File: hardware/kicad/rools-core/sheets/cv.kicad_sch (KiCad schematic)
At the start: 56 parts, among them U4 OPA4171, U5 MCP6004, U6 LM4040DBZ-10, U9 DAC8565

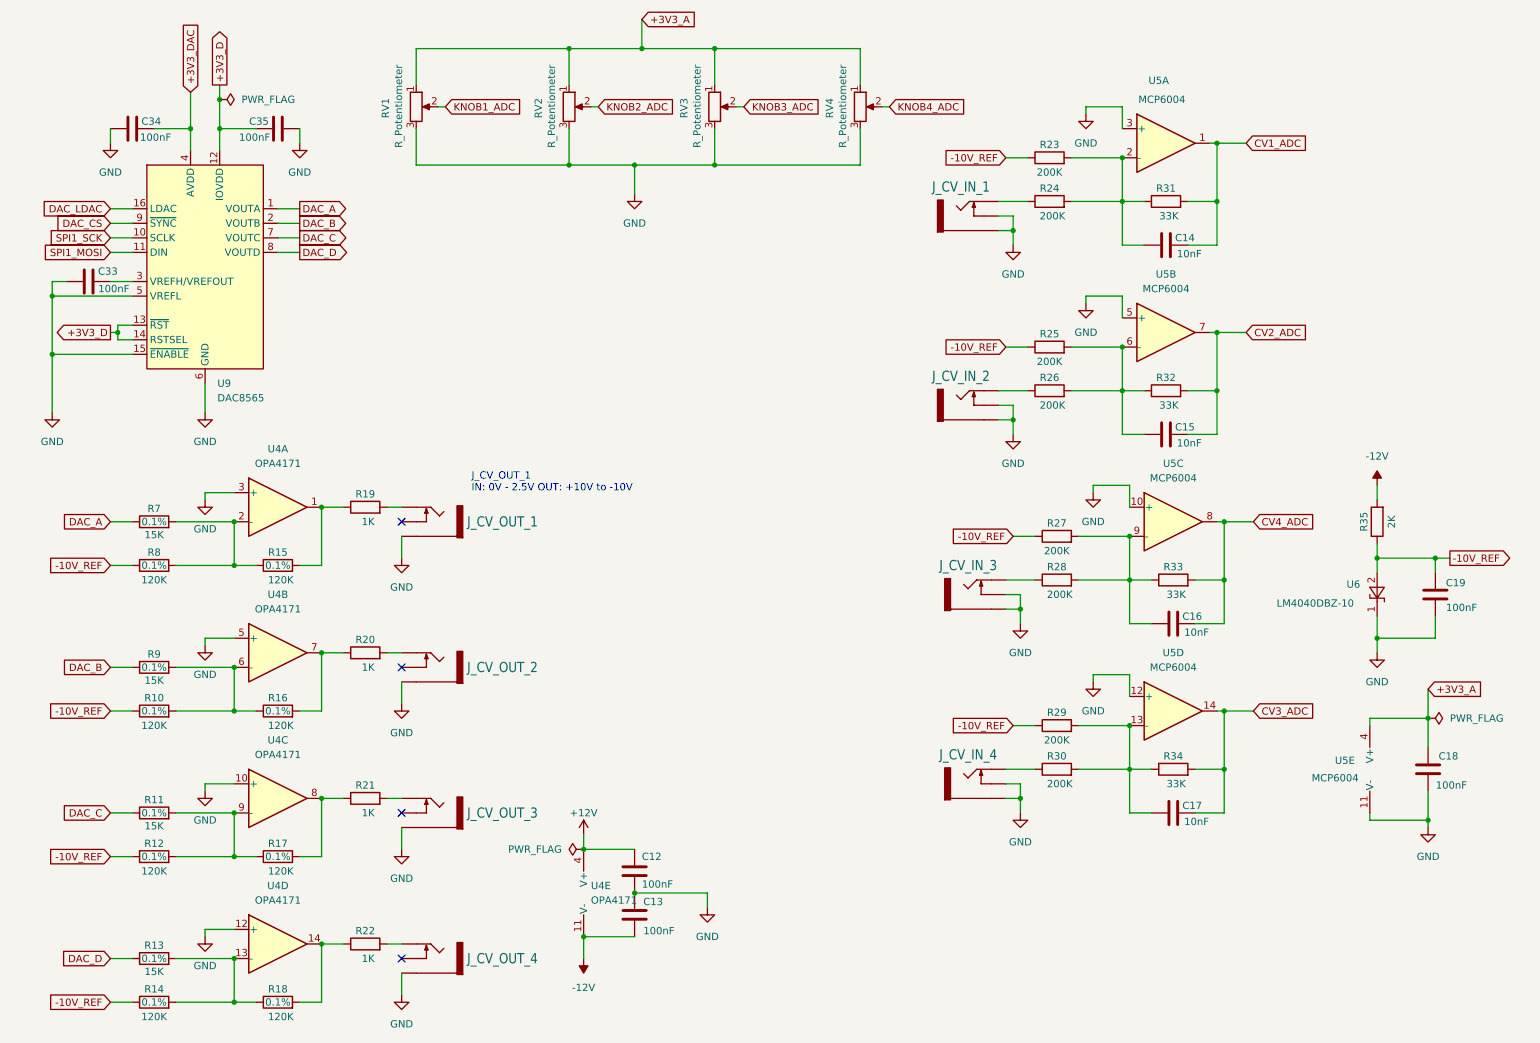
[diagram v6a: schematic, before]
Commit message: Lay out Core front-panel PCB for 10HP Eurorack fit.
Use RK09L 3-pin no-MP pots, split Daisy daughterboard, audio jack refs, and local display footprint library.

Co-authored-by: Cursor <cursoragent@cursor.com>
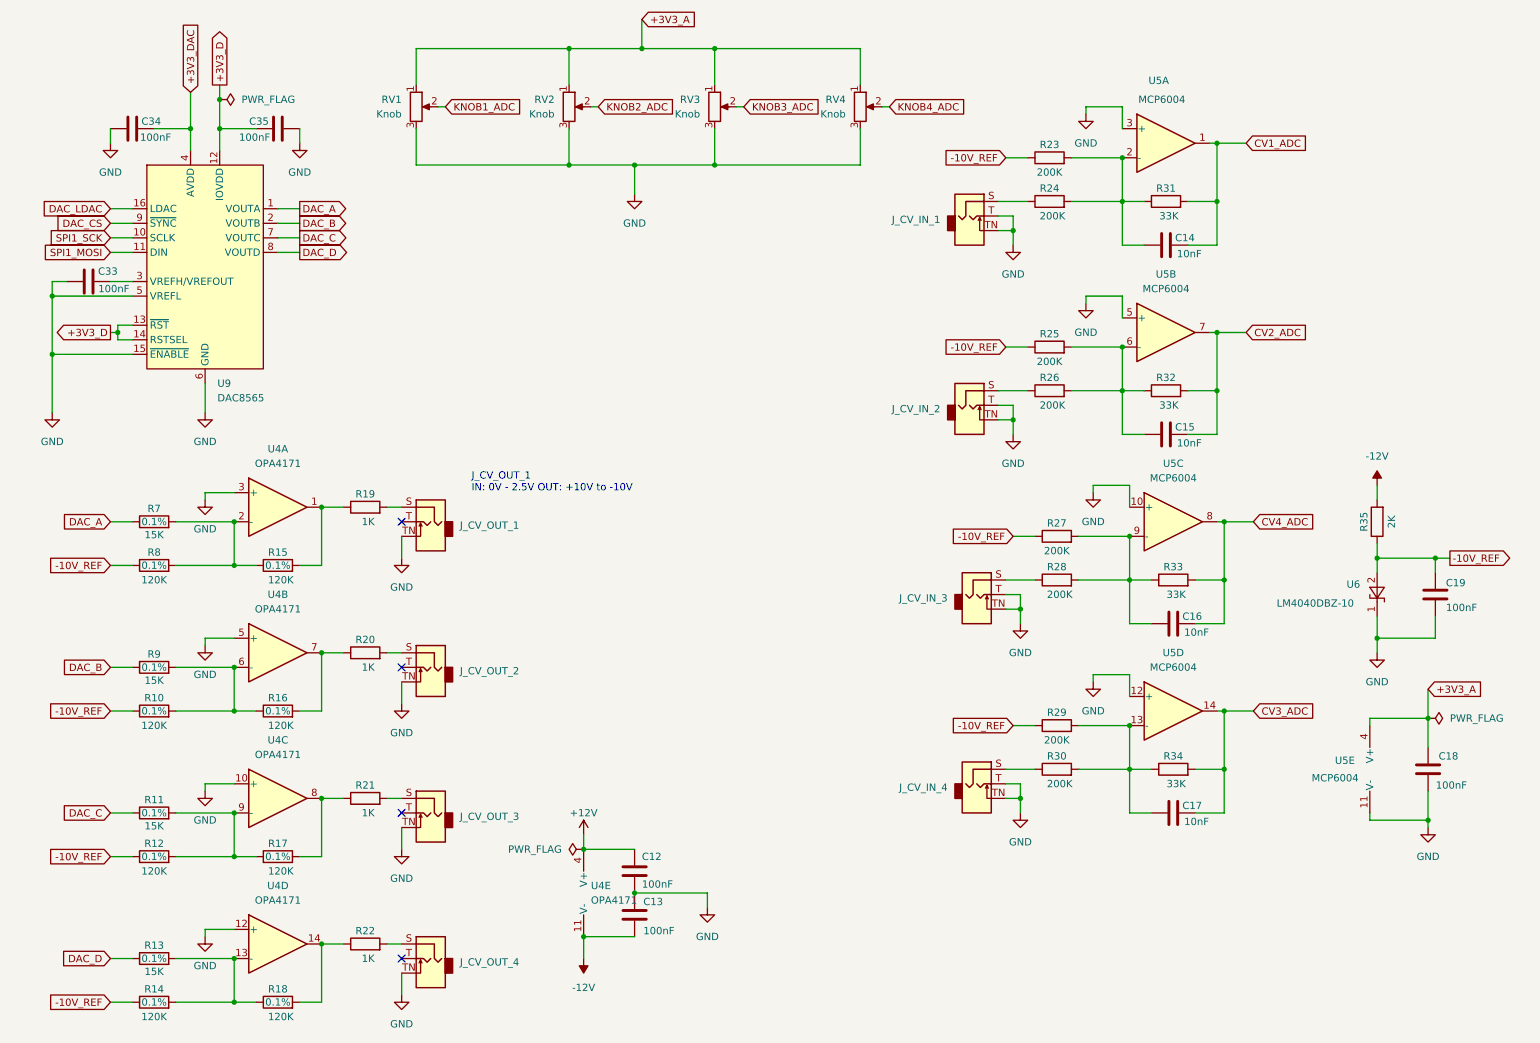
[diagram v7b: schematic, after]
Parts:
- removed J_CV_IN_1, J_CV_IN_2, J_CV_IN_3, J_CV_IN_4, J_CV_OUT_1, J_CV_OUT_2, J_CV_OUT_3, J_CV_OUT_4: (no value), Connector_Audio:Jack_3.5mm_QingPu_WQP-PJ398SM_Vertical_CircularHoles, symbol patch-eagle:EURO_JACK_PJ301M-12
- added J_CV_IN_1, J_CV_IN_2, J_CV_IN_3, J_CV_IN_4, J_CV_OUT_1, J_CV_OUT_2, J_CV_OUT_3, J_CV_OUT_4: AudioJack2_SwitchT, Connector_Audio:Jack_3.5mm_QingPu_WQP-PJ398SM_Vertical_CircularHoles, symbol Connector_Audio:AudioJack2_SwitchT
- RV1, RV2, RV3, RV4: value R_Potentiometer -> Knob; footprint Potentiometer_THT:Potentiometer_Alps_RK09L_Single_Vertical -> Potentiometer_THT:RK09L_3pin_noMP
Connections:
- net GND: now also J_CV_IN_1.T, J_CV_IN_1.TN, J_CV_IN_2.T, J_CV_IN_2.TN, J_CV_IN_3.T, J_CV_IN_3.TN, J_CV_IN_4.T, J_CV_IN_4.TN, J_CV_OUT_1.TN, J_CV_OUT_2.TN, J_CV_OUT_3.TN, J_CV_OUT_4.TN
- net at R22.2: now also J_CV_OUT_4.S
- net at R30.1: now also J_CV_IN_4.S
- net at R24.1: now also J_CV_IN_1.S
- net at R20.2: now also J_CV_OUT_2.S
- net at R26.1: now also J_CV_IN_2.S
- net at R28.1: now also J_CV_IN_3.S
- net at R19.2: now also J_CV_OUT_1.S
- net at R21.2: now also J_CV_OUT_3.S

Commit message: Route Core PCB and place Daisy Seed on the daughterboard.
Sync schematic sheets with the split-board layout and updated interconnects.

Co-authored-by: Cursor <cursoragent@cursor.com>
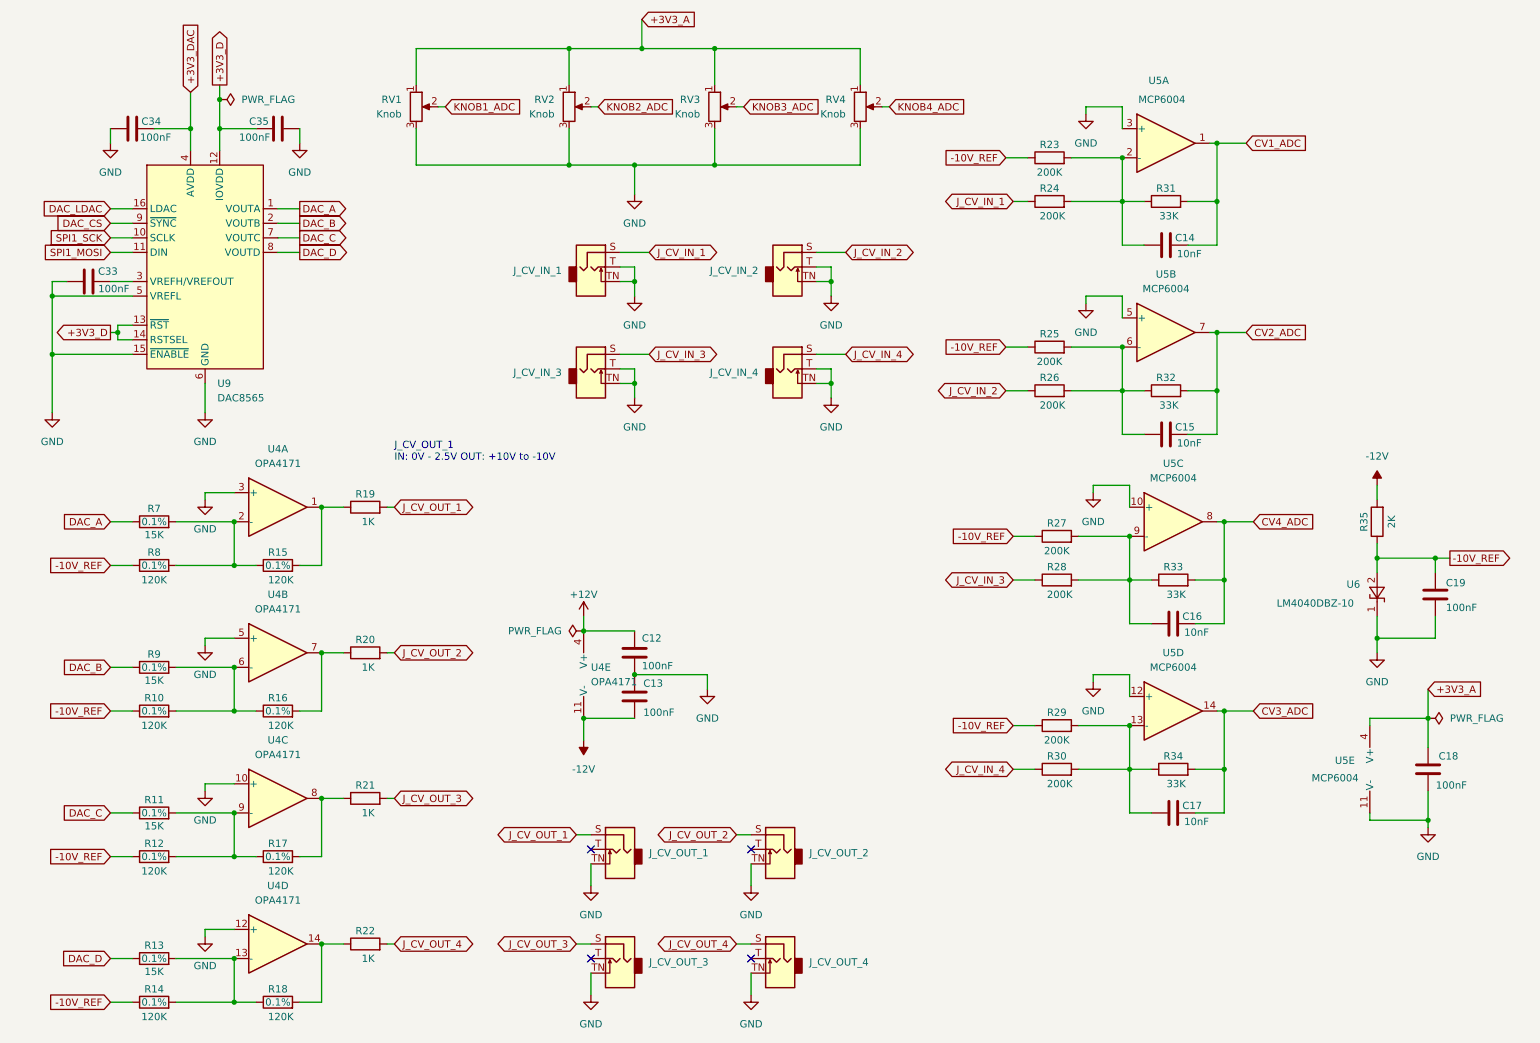
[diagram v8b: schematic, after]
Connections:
- net J_CV_IN_2: now reaches J_CV_IN_2.S, R26.1
- net J_CV_IN_4: now reaches J_CV_IN_4.S, R30.1
- net J_CV_OUT_3: now reaches J_CV_OUT_3.S, R21.2
- net J_CV_IN_1: now reaches J_CV_IN_1.S, R24.1
- net J_CV_OUT_1: now reaches J_CV_OUT_1.S, R19.2
- net J_CV_IN_3: now reaches J_CV_IN_3.S, R28.1
- net J_CV_OUT_2: now reaches J_CV_OUT_2.S, R20.2
- net J_CV_OUT_4: now reaches J_CV_OUT_4.S, R22.2
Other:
- moved on the sheet: C12, C13, J_CV_IN_1, J_CV_IN_2, J_CV_IN_3, J_CV_IN_4, J_CV_OUT_1, J_CV_OUT_2, J_CV_OUT_3, J_CV_OUT_4, U4E
